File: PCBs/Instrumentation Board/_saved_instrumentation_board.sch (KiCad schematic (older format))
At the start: 21 parts, among them J1 Conn_01x02, J2 Conn_01x02, Q1 TEMT6000X01, U1 GPS-ADAFRUIT746, U2 LSM6DS3HTR, U3 LSM6DS3HTR, U4 MS5607-02BA03, U5 MicroSD-ADAFRUIT254

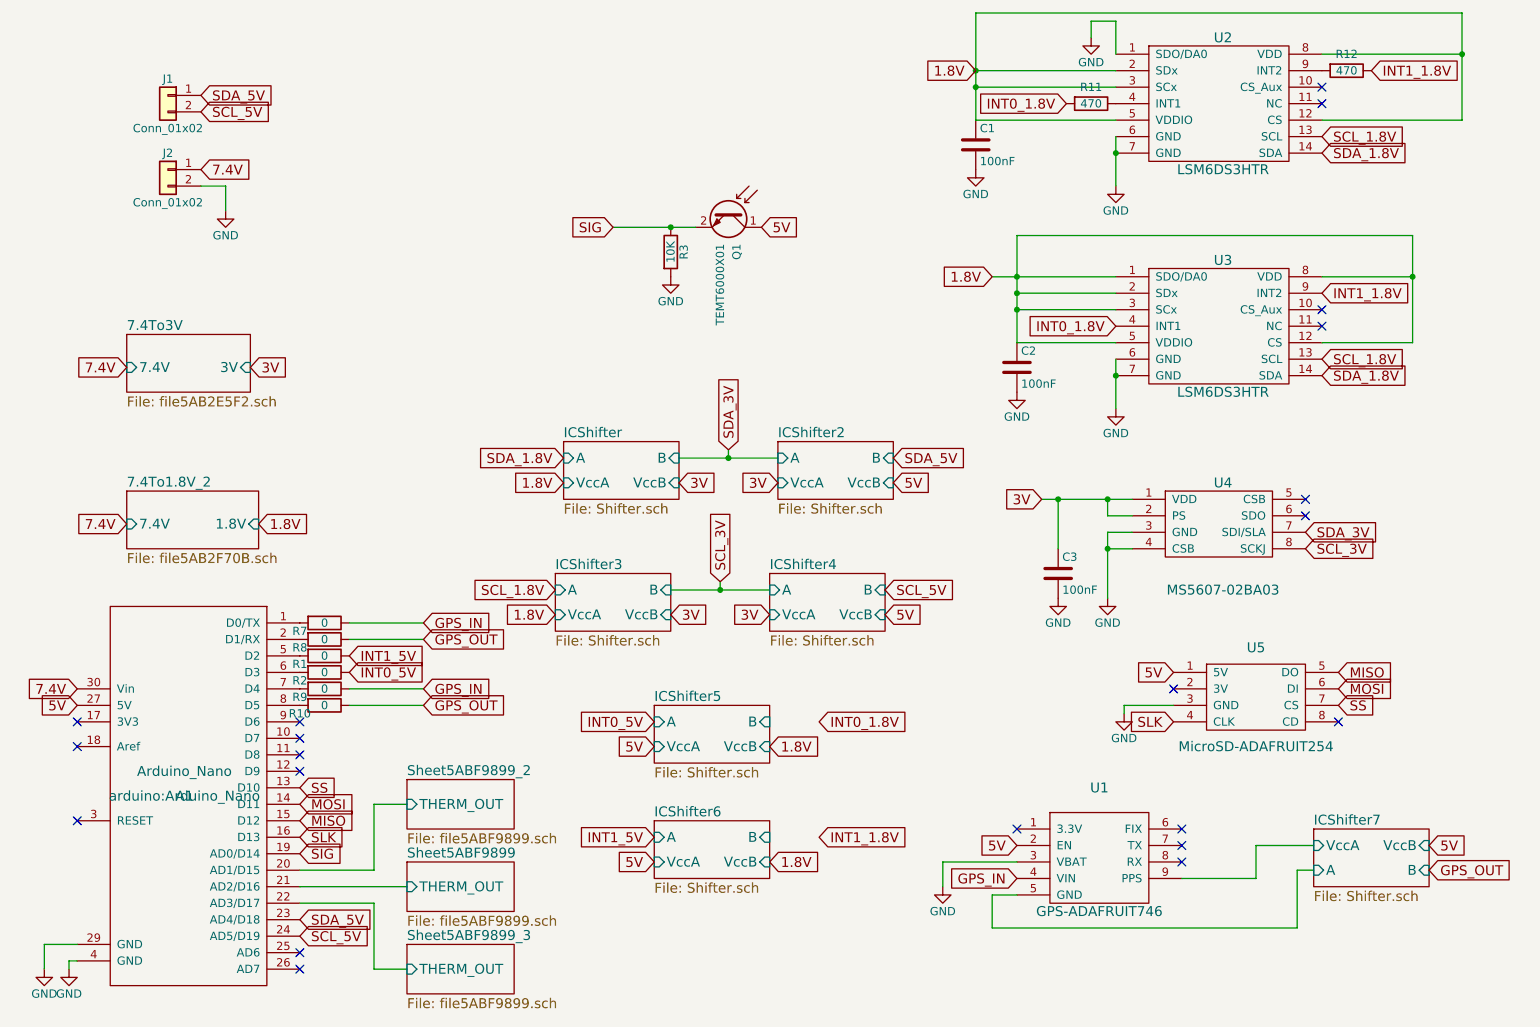
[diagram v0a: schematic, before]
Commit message: Current limiting resistors
Fixed structure of current limiting resistors on instr arduino
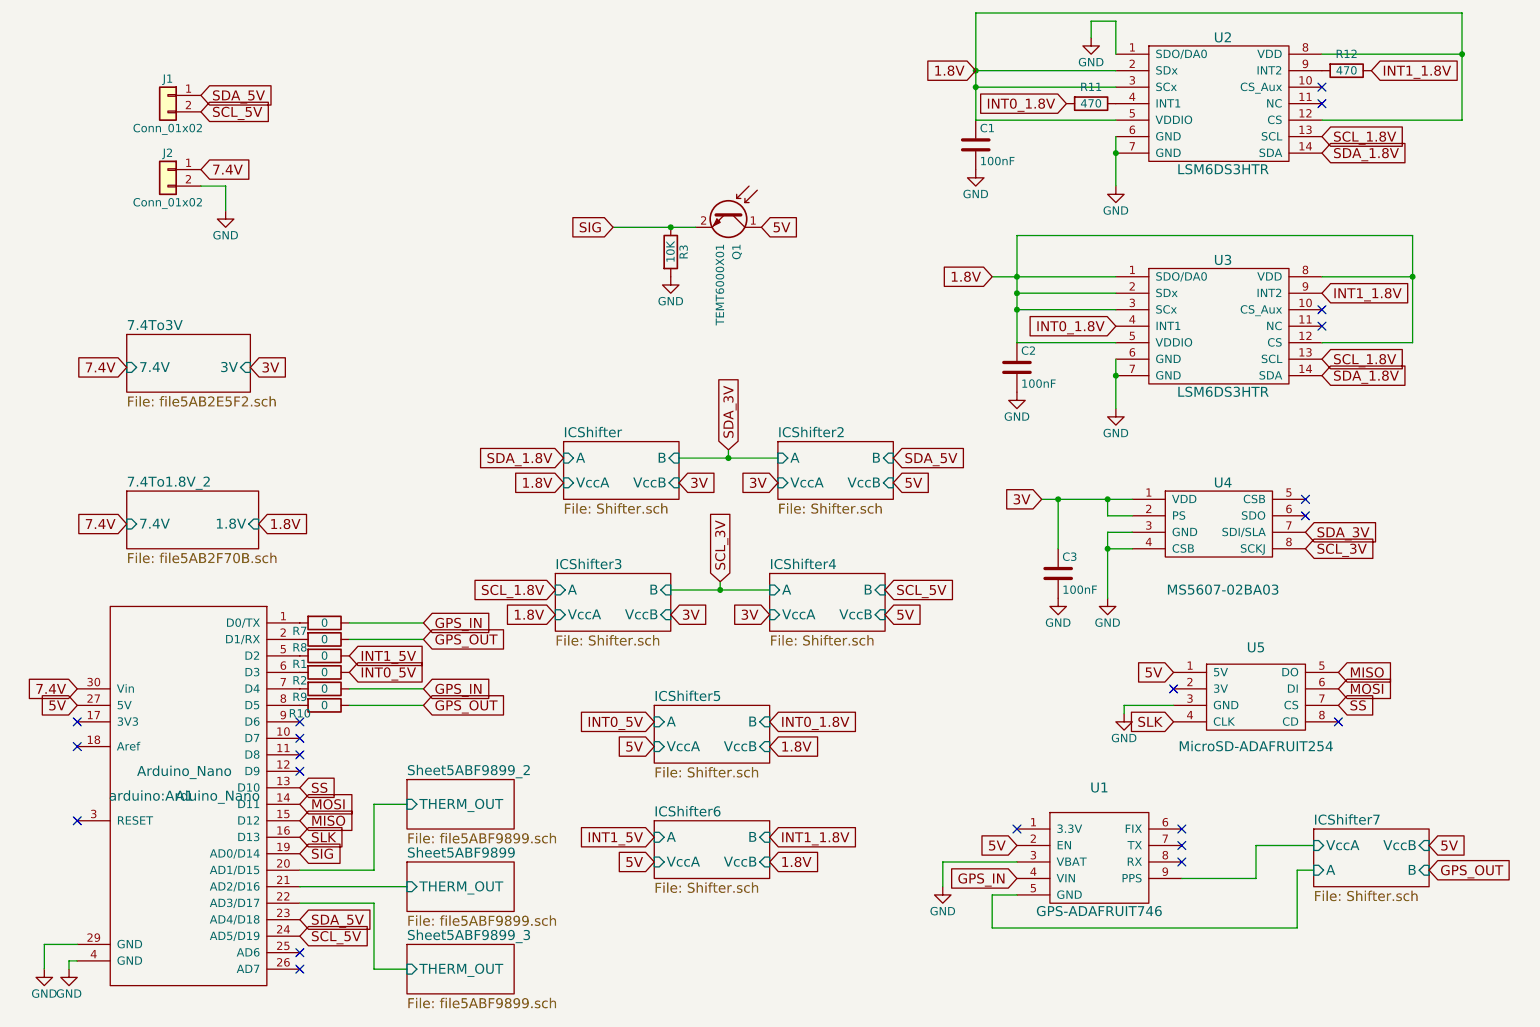
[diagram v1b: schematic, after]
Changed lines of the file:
@@
 Text GLabel 4950 5250 0    60   Input ~ 0
 5V
-Text GLabel 5950 5100 2    60   Input ~ 0
+Text GLabel 5650 5100 2    60   Input ~ 0
 INT0_1.8V
 $Sheet
@@
 Text GLabel 4950 5800 0    60   Input ~ 0
 INT1_5V
-Text GLabel 5950 5800 2    60   Input ~ 0
+Text GLabel 5650 5800 2    60   Input ~ 0
 INT1_1.8V
 Text GLabel 3100 4700 2    60   Input ~ 0
@@
 Connection ~ 7400 3750
 Wire Wire Line
-	7000 2400 7150 2400
-Wire Wire Line
-	7150 2400 7750 2400
+	7000 2400 7750 2400
 Wire Wire Line
 	7600 850  7600 950
@@
 Connection ~ 7750 3000
 Wire Wire Line
-	7750 2900 7750 3000
-Wire Wire Line
-	7750 3000 7750 3200
+	7750 2900 7750 3200
 Wire Wire Line
 	9550 2800 9000 2800
@@
 	7150 2800 7750 2800
 Wire Wire Line
-	9550 2150 9550 2400
-Wire Wire Line
-	9550 2400 9550 2800
+	9550 2150 9550 2800
 Wire Wire Line
 	7150 2150 9550 2150
 Wire Wire Line
-	7150 2150 7150 2400
-Wire Wire Line
-	7150 2400 7150 2500
-Wire Wire Line
-	7150 2500 7150 2600
-Wire Wire Line
-	7150 2600 7150 2800
+	7150 2150 7150 2800
 Connection ~ 6900 1250
 Wire Wire Line
@@
 Connection ~ 6900 1150
 Wire Wire Line
-	6900 1150 6900 1150
-Wire Wire Line
 	6900 1150 7750 1150
 Connection ~ 7750 1650
 Wire Wire Line
-	7750 1550 7750 1650
-Wire Wire Line
-	7750 1650 7750 1850
+	7750 1550 7750 1850
 Wire Wire Line
 	9850 1450 9000 1450
@@
 	6900 1450 7750 1450
 Wire Wire Line
-	9850 800  9850 1050
-Wire Wire Line
-	9850 1050 9850 1450
+	9850 800  9850 1450
 Wire Wire Line
 	6900 800  9850 800
 Wire Wire Line
-	6900 800  6900 1150
-Wire Wire Line
-	6900 1150 6900 1250
-Wire Wire Line
-	6900 1250 6900 1450
+	6900 800  6900 1450
 Wire Wire Line
 	7800 5000 8100 5000
@@
 	7850 4050 7700 4050
 Wire Wire Line
-	7700 3950 7700 4050
-Wire Wire Line
-	7700 4050 7700 4350
+	7700 3950 7700 4350
 Wire Wire Line
 	7850 3950 7700 3950
@@
 	7400 3750 7400 4050
 Wire Wire Line
-	7300 3750 7400 3750
-Wire Wire Line
-	7400 3750 7700 3750
-Wire Wire Line
-	7700 3750 7850 3750
+	7300 3750 7850 3750
 Wire Wire Line
 	1250 6450 1450 6450
@@
 	2200 1850 2350 1850
 Wire Wire Line
-	4700 2100 5050 2100
-Wire Wire Line
-	5050 2100 5200 2100
+	4700 2100 5200 2100
 Connection ~ 5050 2100
 Wire Wire Line
-	5050 4300 5350 4300
-Wire Wire Line
-	5350 4300 5650 4300
+	5050 4300 5650 4300
 Wire Wire Line
 	5350 4300 5350 4250
 Connection ~ 5350 4300
 Wire Wire Line
-	5100 3500 5400 3500
-Wire Wire Line
-	5400 3500 5700 3500
+	5100 3500 5700 3500
 Wire Wire Line
 	5400 3500 5400 3450
